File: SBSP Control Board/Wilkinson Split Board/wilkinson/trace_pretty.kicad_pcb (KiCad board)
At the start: 4 copper layers, 46.4 x 140 mm, 66 parts, among them J1 Conn_01x02_Socket, J10 Conn_Coaxial, J11 Conn_Coaxial, J12 Conn_Coaxial, J13 Conn_Coaxial, J14 Conn_Coaxial, J15 Conn_Coaxial, J16 Conn_Coaxial, J2 Conn_01x02_Socket, J20 Conn_Coaxial, J9 Conn_Coaxial, U1 ADAR1000ACCZN, U2 SN74AVC4T245PW, U3 SN74AVC4T245PW, U4 ADAR1000ACCZN

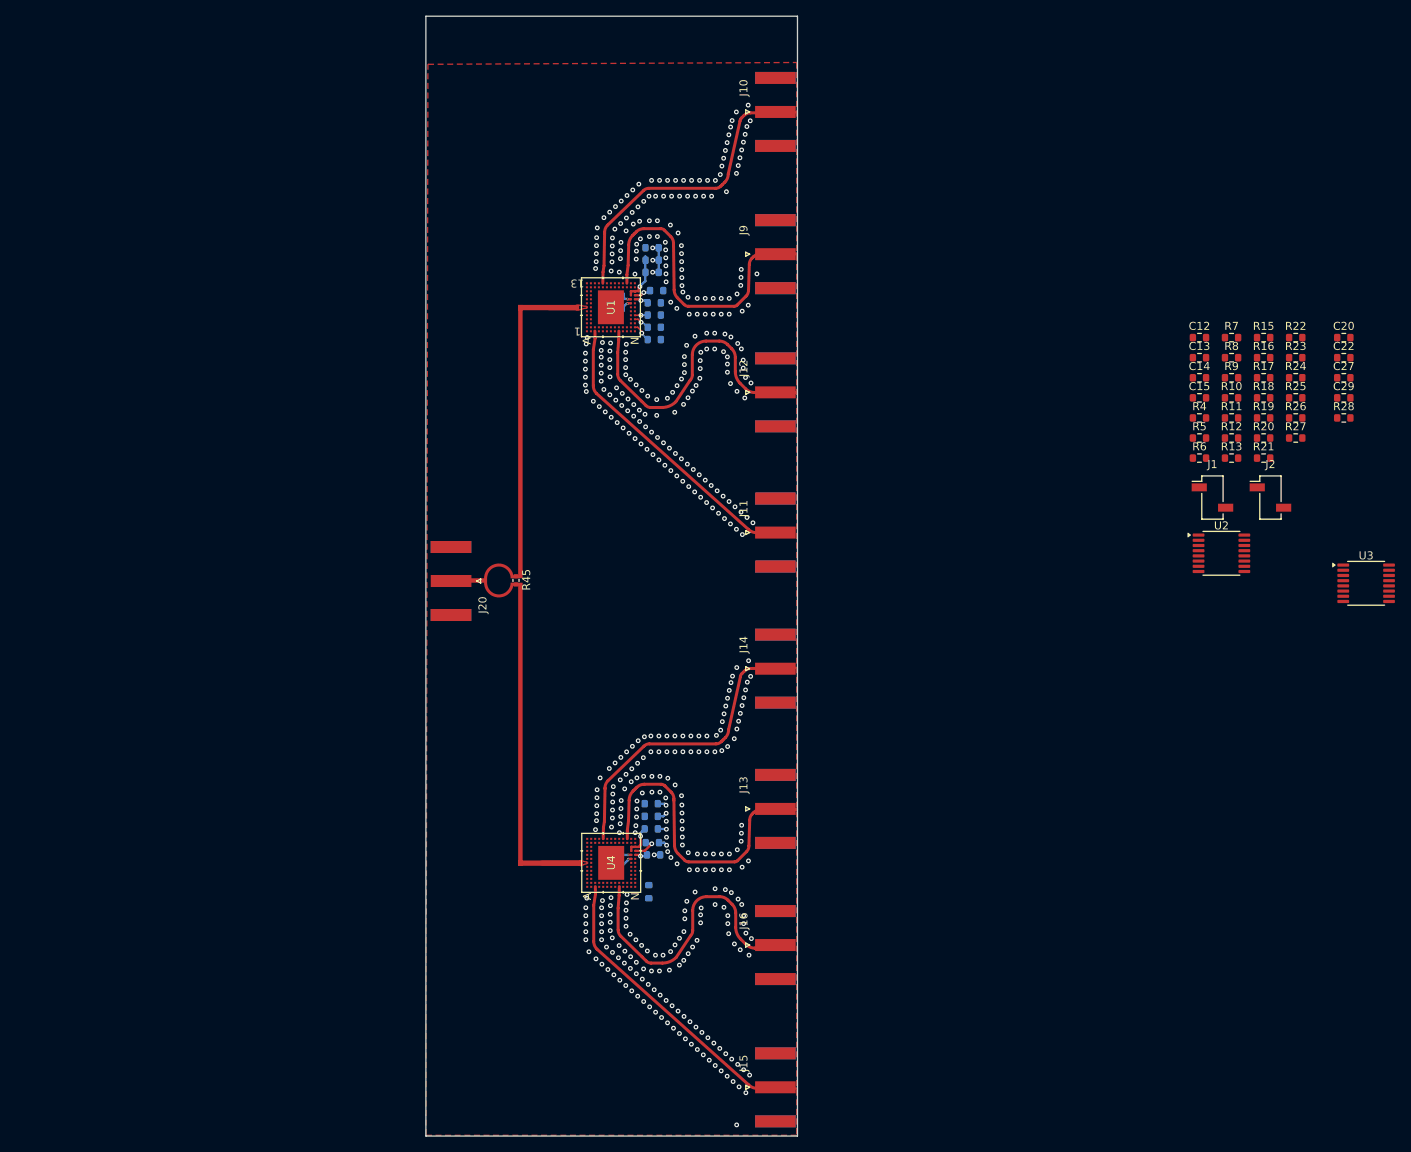
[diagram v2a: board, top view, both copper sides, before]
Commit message: finished schematic and routing rev1
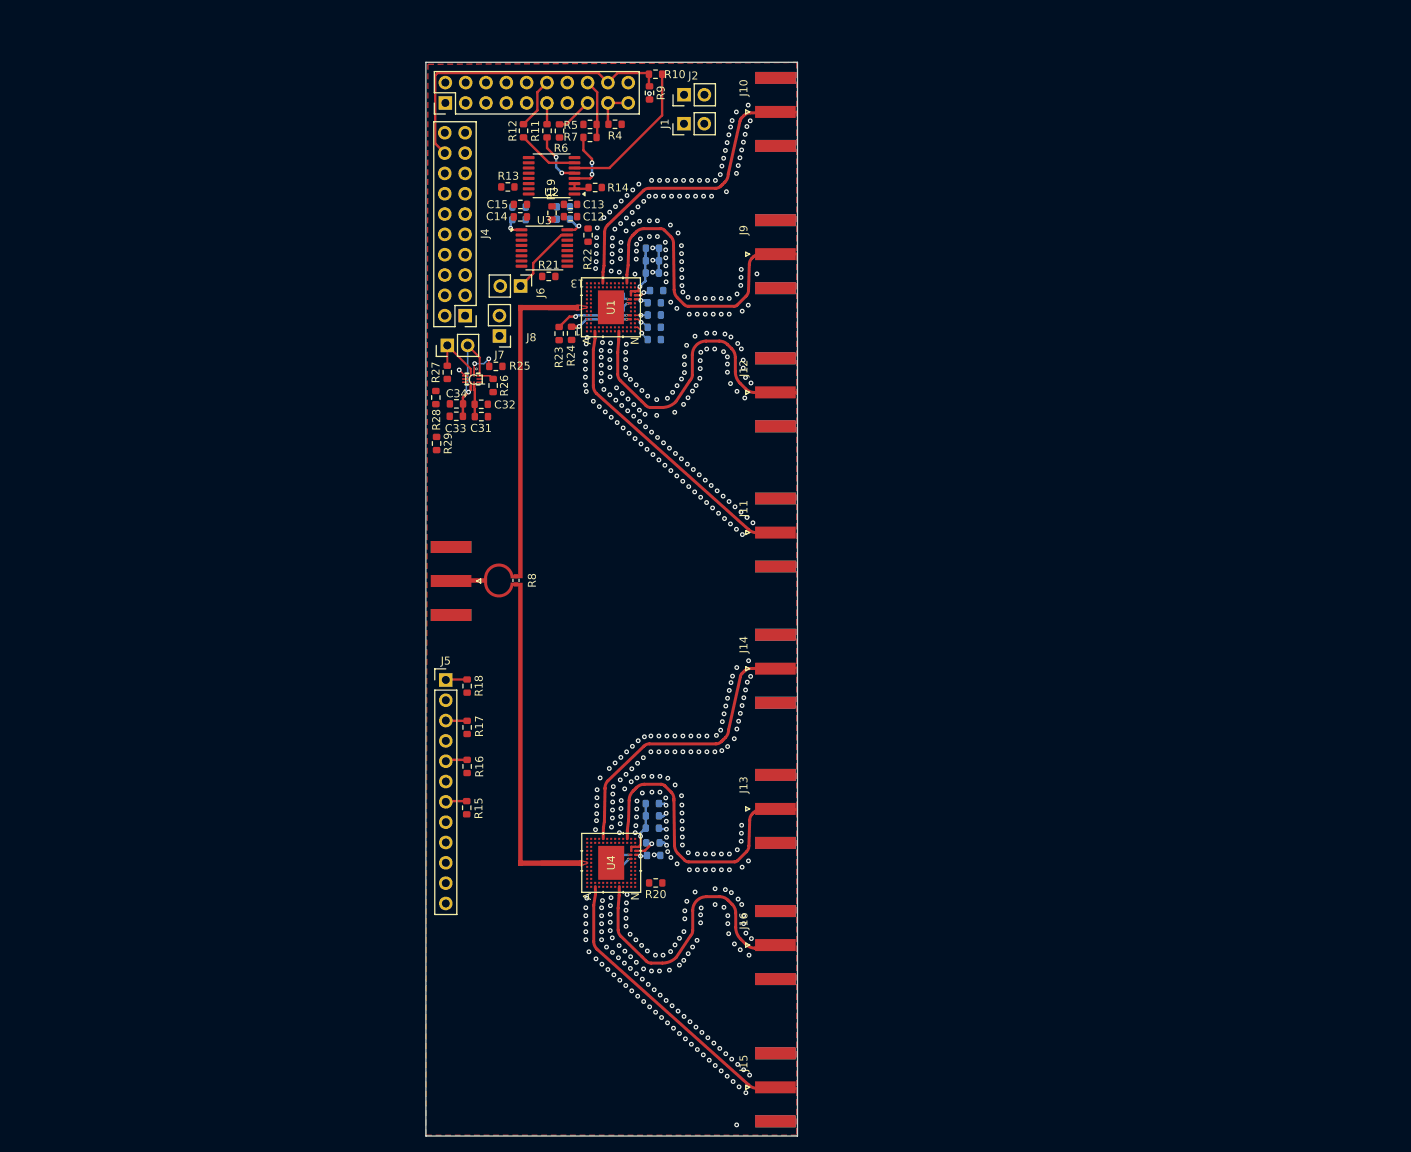
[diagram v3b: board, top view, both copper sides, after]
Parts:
- added C31: 10pF, Resistor_SMD:R_0603_1608Metric, F.Cu at (423.4, 105.1)
- added C32: 0.1uF, Resistor_SMD:R_0603_1608Metric, F.Cu at (423.4, 103.6)
- added C33: 10pF, Resistor_SMD:R_0603_1608Metric, F.Cu at (420.2, 105.1)
- added C34: 0.1uF, Resistor_SMD:R_0603_1608Metric, F.Cu at (420.3, 103.5)
- added IC1: SN74AVC2T245RSWR, little foot:RSW_RPUQFNN10_, F.Cu at (422.3, 100.4)
- added J3: Conn_01x20_Socket, Connector_PinHeader_2.54mm:PinHeader_2x10_P2.54mm_Vertical, F.Cu at (418.9, 65.9)
- added J4: Conn_01x20_Socket, Connector_PinHeader_2.54mm:PinHeader_2x10_P2.54mm_Vertical, F.Cu at (421.4, 92.5)
- added J5: Conn_01x12_Socket, Connector_PinHeader_2.54mm:PinHeader_1x12_P2.54mm_Vertical, F.Cu at (418.9, 138.1)
- added J6: Conn_01x02_Pin, Connector_PinHeader_2.54mm:PinHeader_1x02_P2.54mm_Vertical, F.Cu at (428.3, 88.8)
- added J7: Conn_01x02_Pin, Connector_PinHeader_2.54mm:PinHeader_1x02_P2.54mm_Vertical, F.Cu at (425.6, 95.1)
- added J8: Conn_01x02_Pin, Connector_PinHeader_2.54mm:PinHeader_1x02_P2.54mm_Vertical, F.Cu at (419.1, 96.2)
- C16: renamed from C20; moved to B.Cu
- C22, C27, C29: moved to B.Cu
- J1, J2: footprint Connector_PinSocket_2.54mm:PinSocket_1x02_P2.54mm_Vertical_SMD_Pin1Left -> Connector_PinHeader_2.54mm:PinHeader_1x02_P2.54mm_Vertical
- R15: renamed from R14; moved to F.Cu
- moved R16 113.1 mm to (421.6, 148.9), turned to 90 degrees
- moved U3 110.9 mm to (431.3, 84.1)
- moved R17 109.8 mm to (421.6, 144.0), turned to 90 degrees
- moved R28 107.5 mm to (417.7, 102.8), turned to -90 degrees
- moved R29 107.4 mm to (417.8, 108.5), turned to -90 degrees
- moved R18 106.8 mm to (421.6, 138.8), turned to 90 degrees
- moved R27 106.1 mm to (419.1, 99.6), turned to 90 degrees
- moved C27 104.1 mm to (444.8, 158.4)
- moved R20 103.8 mm to (445.2, 163.4), turned to 180 degrees
- moved C29 103.5 mm to (444.9, 160.0)
- moved R26 100.3 mm to (424.9, 101.2), turned to 90 degrees
- moved R25 100.0 mm to (425.2, 98.9), turned to 180 degrees
- moved U2 96.1 mm to (432.2, 75.0), turned to 180 degrees
- moved R13 95.8 mm to (426.7, 76.4), turned to 180 degrees
- moved R12 95.5 mm to (428.6, 69.4), turned to -90 degrees
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- renumbered C16 to C17, C17 to C18, C21 to C19, C18 to C20, C19 to C21, J20 to J17, R9 to R10, R10 to R11, R11 to R12, R12 to R13, R13 to R14, R15 to R16, R16 to R17, R17 to R18, R18 to R19, R28 to R20, R19 to R21, R20 to R22, R21 to R23, R22 to R24, R23 to R25, R24 to R26, R25 to R27, R26 to R28, R27 to R29, R45 to R8, R8 to R9
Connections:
- U4 pad M3: ADAR_CS_STAGE2_1V8 -> /CSB
- U4 pad M4: ADAR_SDO_STAGE2_1V8 -> ADAR_SDO_STAGE1_1V8
- U4 pad M6: ADAR_SCLK_1V8 -> /SCLK
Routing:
- net /SPI_SEL_A: track 0.00 -> 39.7 mm
- net Net-(U2-2A1): track 0.00 -> 18.8 mm
- net +1.8V: track 5.81 -> 19.1 mm, vias 2 -> 3
- net ADAR_SDIO_1V8: track 0.00 -> 9.46 mm, vias 0 -> 2
- net Net-(J6-Pin_1): track 0.00 -> 9.24 mm
- net ADAR_SDO_STAGE1_1V8: track 0.00 -> 7.88 mm, vias 0 -> 2
- net Net-(U2-2A2): track 0.00 -> 7.69 mm
- net Net-(U2-1A1): track 0.00 -> 7.63 mm, vias 0 -> 2
- net /SPI_CLK: track 0.00 -> 7.38 mm
- net +3.3V: track 7.49 -> 14.8 mm, vias 2 -> 4
- net Net-(IC1-~{OE2}): track 0.00 -> 7.09 mm
- net Net-(U2-1A2): track 0.00 -> 6.80 mm, vias 0 -> 2
- net /GPIO3: track 0.00 -> 6.41 mm
- net /SPI_MOSI: track 0.00 -> 5.24 mm
- net Net-(J3-Pin_15): track 0.00 -> 4.62 mm, vias 0 -> 1
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- added copper zone on F.Cu, net +1.8V
- added copper zone on F.Cu, net +3V3
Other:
- board size 46.4 x 140 mm -> 46.4 x 134.2 mm

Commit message: gave to fayed for sims
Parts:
- moved R10 93.1 mm to (374.2, 122.7), turned to 90 degrees
- moved J3 92.6 mm to (377.8, 148.9), turned to 180 degrees
- moved J15 90.9 mm to (500.9, 107.7), turned to 90 degrees
- moved J10 90.8 mm to (379.0, 107.7), turned to 90 degrees
- moved J2 90.0 mm to (376.8, 119.1), turned to 180 degrees
- moved R9 89.7 mm to (376.6, 123.4), turned to 0 degrees
- moved J1 85.0 mm to (380.4, 119.1), turned to 180 degrees
- moved R12 84.3 mm to (381.3, 139.2), turned to 0 degrees
- moved R5 84.0 mm to (380.5, 130.9), turned to 90 degrees
- moved R4 83.9 mm to (380.5, 127.7), turned to -90 degrees
- moved R11 83.6 mm to (381.3, 136.2), turned to 0 degrees
- moved R6 83.3 mm to (381.3, 134.7), turned to 0 degrees
- moved R7 81.7 mm to (382.1, 130.9), turned to -90 degrees
- moved U2 75.6 mm to (386.9, 135.7), turned to -90 degrees
- moved R13 75.2 mm to (388.3, 141.1), turned to -90 degrees
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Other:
- board size 46.4 x 134.2 mm -> 134.2 x 46.4 mm

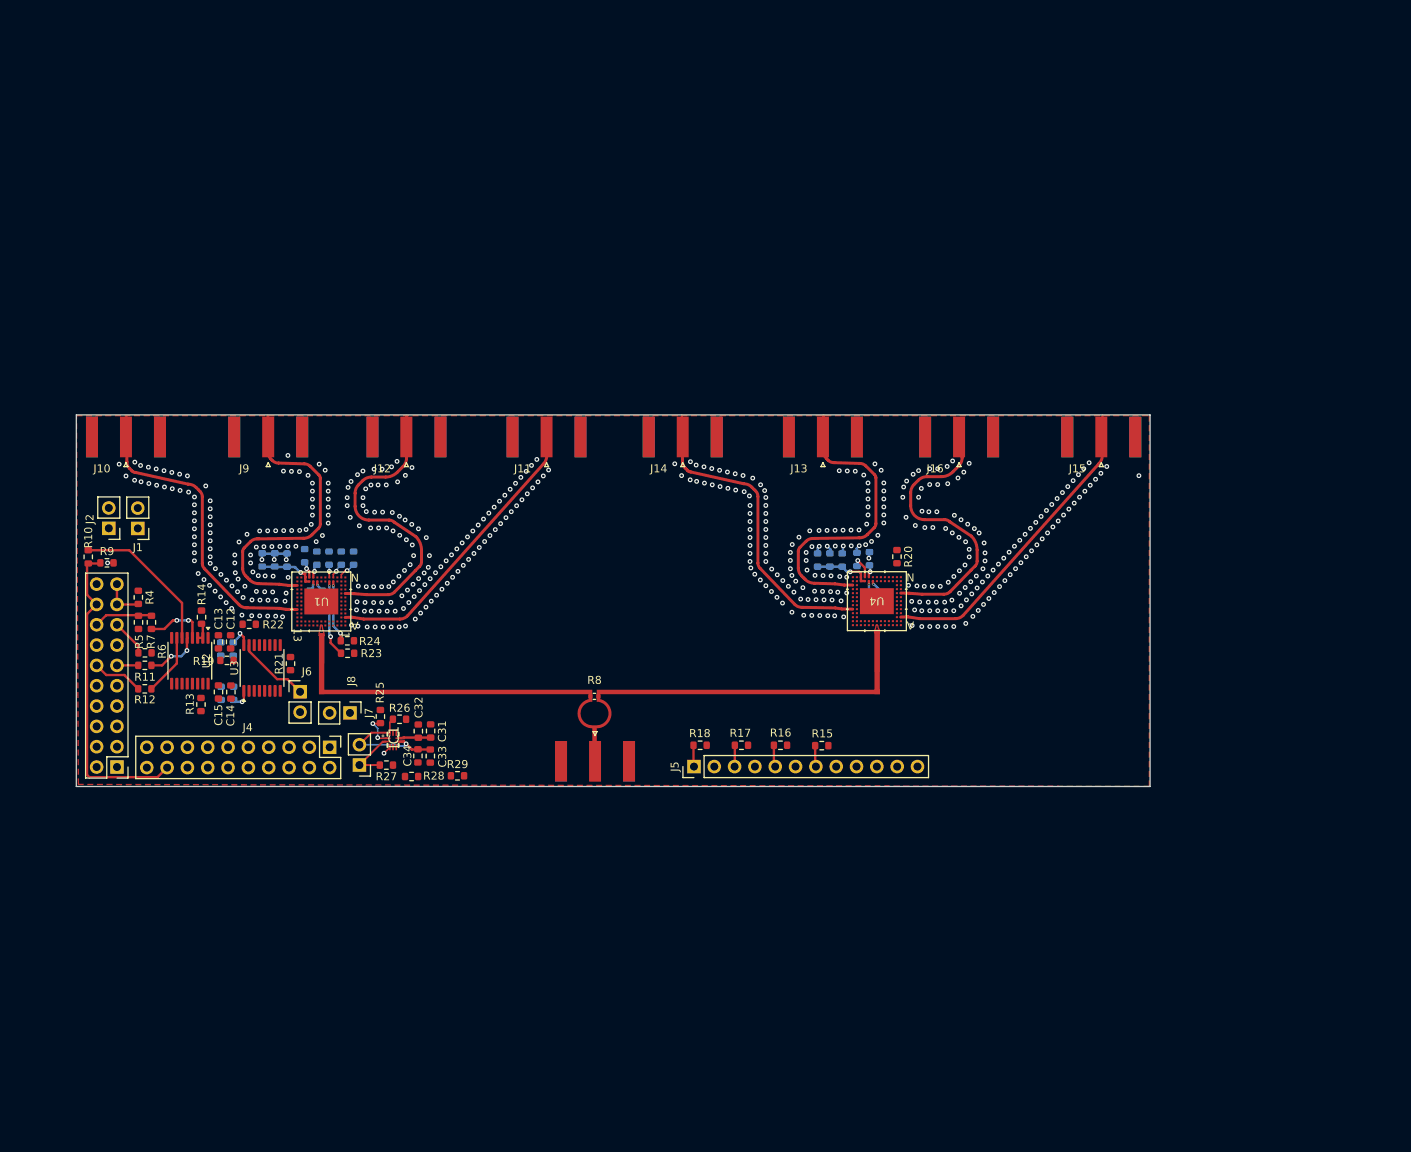
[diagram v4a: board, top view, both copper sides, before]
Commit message: redid entire layout for support
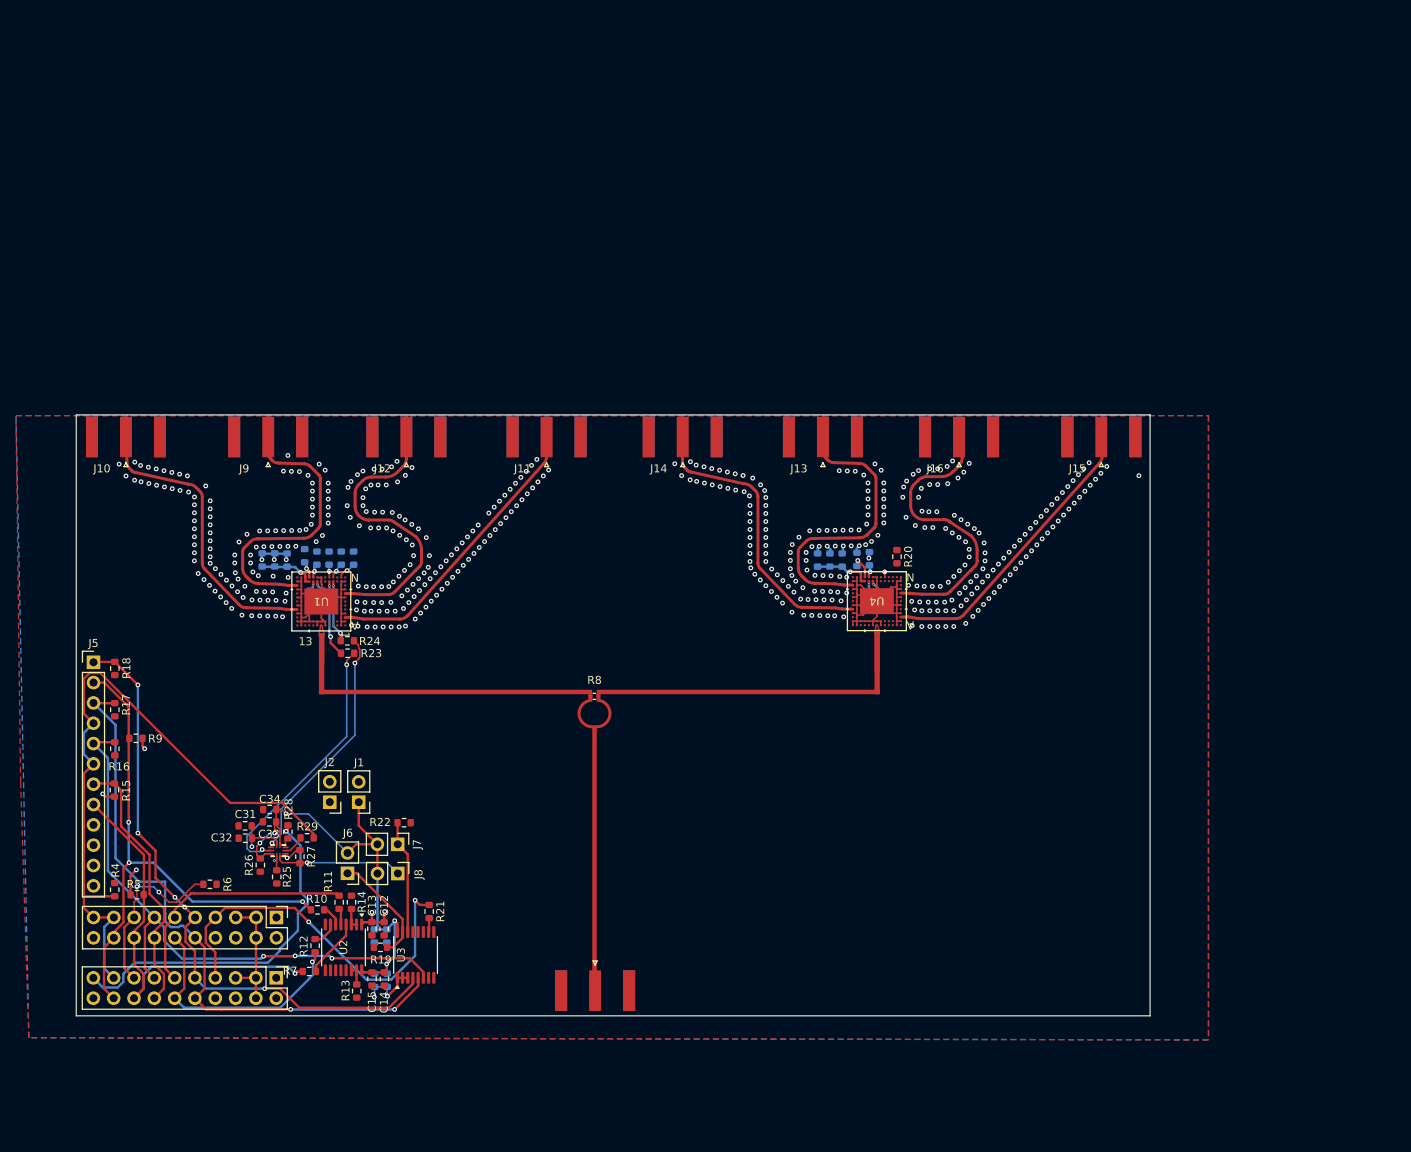
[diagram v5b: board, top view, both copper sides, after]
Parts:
- moved R15 88.6 mm to (377.5, 151.8), turned to 90 degrees
- moved R16 83.2 mm to (377.6, 146.7), turned to 90 degrees
- moved R17 78.5 mm to (377.6, 141.8), turned to 90 degrees
- moved J5 76.2 mm to (374.9, 135.8), turned to 0 degrees
- moved R18 73.8 mm to (377.6, 136.6), turned to 90 degrees
- moved R10 52.6 mm to (402.9, 166.8), turned to 0 degrees
- moved R7 47.9 mm to (401.9, 174.5), turned to 0 degrees
- moved J1 44.0 mm to (408.1, 153.3)
- moved J2 44.0 mm to (404.4, 153.3)
- moved R13 40.8 mm to (407.8, 176.9)
- moved C12 40.7 mm to (411.2, 169.2)
- moved C13 40.7 mm to (409.7, 169.2)
- moved C14 40.7 mm to (411.3, 175.4)
- moved C15 40.7 mm to (409.7, 175.4)
- moved C17 40.7 mm to (410.0, 175.6)
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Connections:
- C12 pad 2: +3V3 -> +3.3V
- C13 pad 2: +3V3 -> +3.3V
- C17 pad 2: +3V3 -> +3.3V
- C18 pad 2: +3V3 -> +3.3V
- C31 pad 2: +3V3 -> +3.3V
- C32 pad 2: +3V3 -> +3.3V
- IC1 pad 7: +3V3 -> +3.3V
- R9 pad 2: +3V3 -> +3.3V
- U2 pad 1: +3V3 -> +3.3V
- U3 pad 1: +3V3 -> +3.3V
- U3 pad 2: +3V3 -> +3.3V
- U3 pad 3: +3V3 -> +3.3V
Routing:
- net GND: track 11.6 -> 108.1 mm, vias 482 -> 486
- net /SPI_MOSI: track 5.24 -> 85.1 mm
- net /GPIO1: track 2.68 -> 79.6 mm, vias 0 -> 2
- net /GPIO0: track 2.69 -> 78.1 mm, vias 0 -> 5
- net /GPIO4: track 2.74 -> 74.6 mm, vias 0 -> 3
- net /AVDD2: track 0.00 -> 47.9 mm, vias 0 -> 2
- net /SPI_CLK: track 7.38 -> 52.5 mm, vias 0 -> 1
- net /SPI_MISO: track 0.00 -> 44.6 mm, vias 0 -> 1
- net +1.8V: track 19.1 -> 59.3 mm, vias 3 -> 6
- net Net-(IC1-A2): track 0.00 -> 33.3 mm, vias 0 -> 2
- net /GPIO5: track 2.65 -> 33.5 mm
- net Net-(IC1-A1): track 0.00 -> 30.8 mm, vias 0 -> 2
- net /SPI_SEL_A: track 39.7 -> 69.0 mm, vias 0 -> 3
- net /GPIO2: track 2.66 -> 31.0 mm
- net /GPIO3: track 6.41 -> 31.1 mm, vias 0 -> 1
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- added copper zone on In2.Cu, net +3.3V
- added copper zone on B.Cu, net GND
- removed copper zone on F.Cu, net +1.8V
- removed copper zone on F.Cu, net +3V3
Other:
- board size 134.2 x 46.4 mm -> 134.2 x 75.1 mm

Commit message: worked on confirming DRC errors and fixing layout
10-2

finished up re-design with new layout for the improved signal integrity and also started working on DRC errors. the DRC info is from JLC BUT their capabilities are general enough it provides a good glimpse into what exactly manufacteres will be able to do, so that when we do go to whoever we use (mid atlantic?), we'll at least have a general idea of what we can vs cannot do. This may require adjusting via sizes or changing spacing, but in general, adhering to at least JLC's specs should put us in a decent place. I also, minimally, worked on the PLL schematic and worked on finishing that so we can begin layout.
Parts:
- moved R20 4.10 mm to (478.9, 124.6), turned to 180 degrees
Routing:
- net /CSB: track 0.00 -> 139.5 mm, vias 0 -> 7
- net /SCLK: track 0.00 -> 135.4 mm, vias 0 -> 7
- net ADAR_TR_1V8: track 0.00 -> 98.7 mm, vias 0 -> 2
- net +1.8V: track 59.3 -> 154.7 mm, vias 6 -> 8
- net ADAR_TX_LOAD_1V8: track 0.00 -> 92.4 mm, vias 0 -> 2
- net ADAR_SDIO_1V8: track 9.46 -> 83.9 mm, vias 2 -> 3
- net ADAR_SDO_STAGE1_1V8: track 7.88 -> 81.2 mm, vias 2 -> 3
- net /GPIO5: track 33.5 -> 70.8 mm, vias 0 -> 2
- net /AVDD: track 17.7 -> 33.1 mm
- net GND: track 108.1 -> 117.8 mm, vias 486 -> 494
- net PLL_IN: track 8.26 -> 0.01 mm
- net OUT7: track 39.5 -> 34.5 mm
- net OUT5: track 39.5 -> 35.0 mm
- net OUT1: track 39.5 -> 35.0 mm
- net OUT3: track 39.1 -> 35.3 mm
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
